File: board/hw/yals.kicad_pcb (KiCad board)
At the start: 2 copper layers, 30 parts, among them J1 SWD, J2 UART, U1 RP2040, U2 M24C02-FMN, U3 MCP1703Ax-330xxTT, U4 W25Q32JVSS, Y1 Crystal

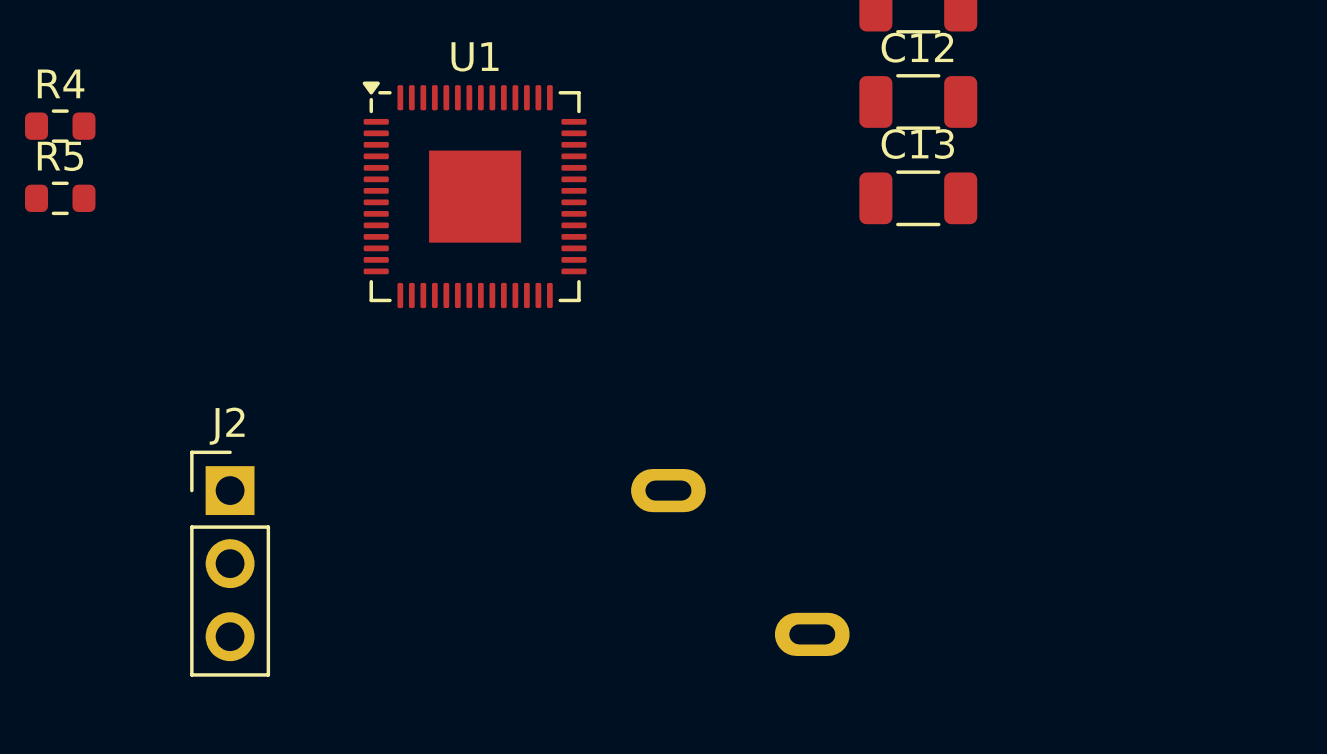
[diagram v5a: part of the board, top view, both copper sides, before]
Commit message: added engine driver with votage measuring resistor to schematics
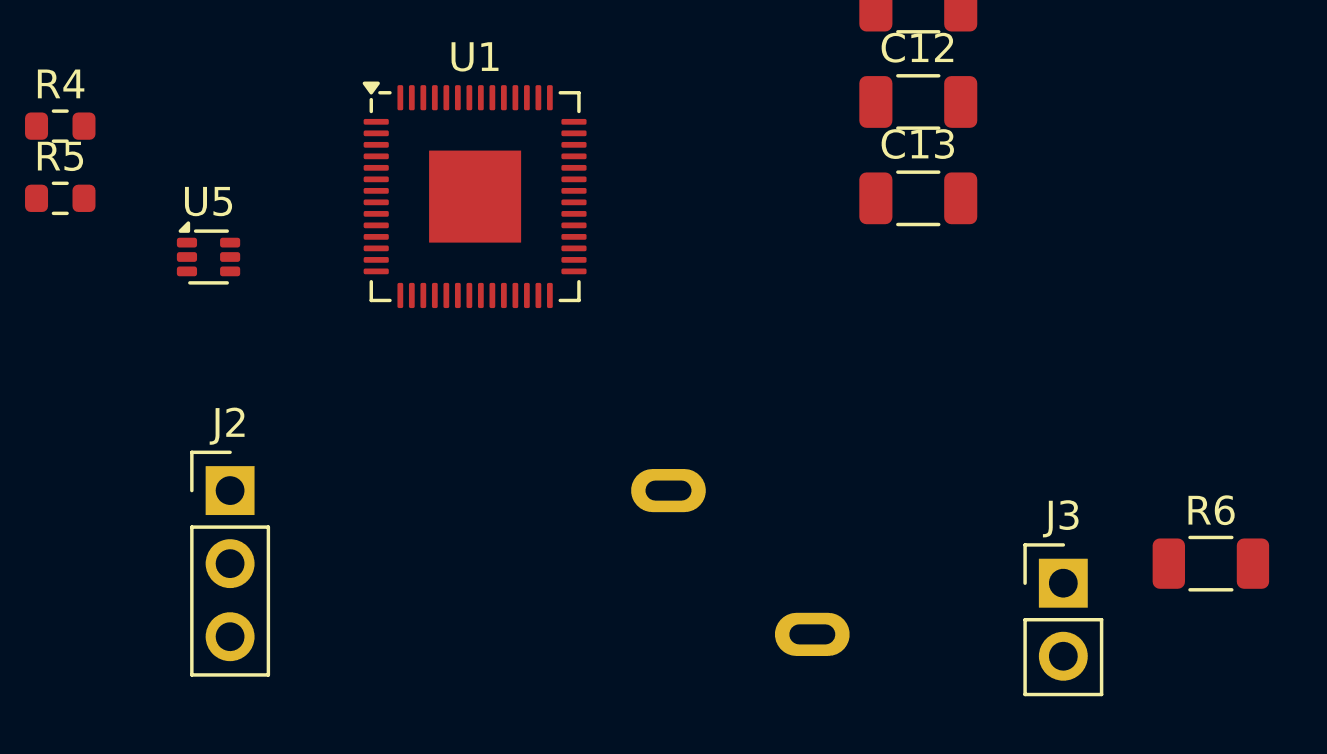
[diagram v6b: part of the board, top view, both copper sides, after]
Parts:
- added J3: eng, Connector_PinHeader_2.54mm:PinHeader_1x02_P2.54mm_Vertical, F.Cu at (183.9, 87.0)
- added R6: 0.01R, Resistor_SMD:R_1206_3216Metric, F.Cu at (189.0, 86.4)
- added U5: DRV8220, Package_TO_SOT_SMD:SOT-563, F.Cu at (154.2, 75.7)
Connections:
- U1 pad 4: /microcontroller/engine_IN1 -> /engine ctrl/eng_IN1
- U1 pad 5: /microcontroller/engine_IN2 -> /engine ctrl/eng_IN2

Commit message: fixed feedback pins directions
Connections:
- U1 pad 40: unconnected-(U1-GPIO28_ADC2-Pad40) -> /microcontroller/eng_current_feedback
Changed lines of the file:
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@@
   (net 23 "Net-(U1-QSPI_SD3)")
   (net 24 "/engine ctrl/eng_Vcc_feedback")
-  (net 25 "unconnected-(U1-GPIO28_ADC2-Pad40)")
+  (net 25 "/microcontroller/eng_current_feedback")
   (net 26 "unconnected-(U1-GPIO29_ADC3-Pad41)")
   (net 27 "unconnected-(U1-USB_DM-Pad46)")
@@
       (net 24 "/engine ctrl/eng_Vcc_feedback") (pinfunction "GPIO27_ADC1") (pintype "bidirectional"))
     (pad "40" smd roundrect (at 3.4375 -1.8) (size 0.875 0.2) (layers "F.Cu" "F.Paste" "F.Mask") (roundrect_rratio 0.25)
-      (net 25 "unconnected-(U1-GPIO28_ADC2-Pad40)") (pinfunction "GPIO28_ADC2") (pintype "bidirectional"))
+      (net 25 "/microcontroller/eng_current_feedback") (pinfunction "GPIO28_ADC2") (pintype "bidirectional"))
     (pad "41" smd roundrect (at 3.4375 -2.2) (size 0.875 0.2) (layers "F.Cu" "F.Paste" "F.Mask") (roundrect_rratio 0.25)
       (net 26 "unconnected-(U1-GPIO29_ADC3-Pad41)") (pinfunction "GPIO29_ADC3") (pintype "bidirectional"))

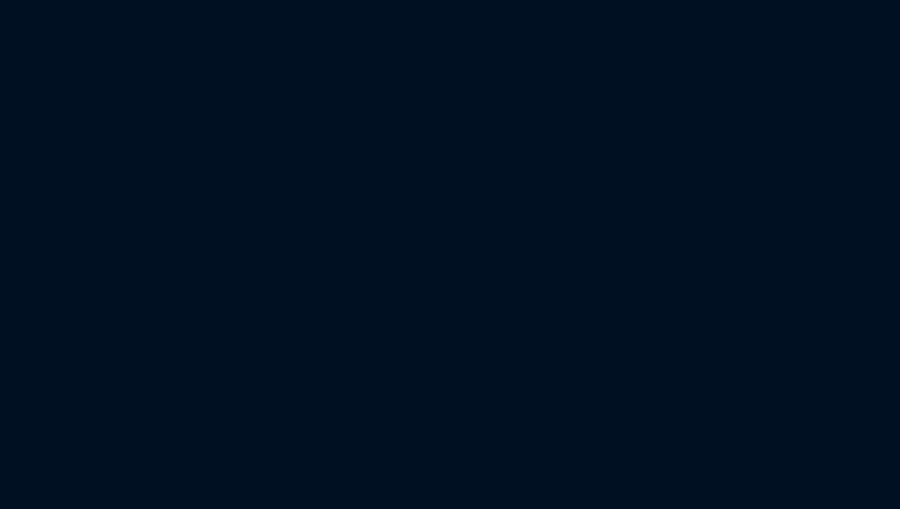
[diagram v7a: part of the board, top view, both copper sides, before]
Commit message: added current measuing circuit
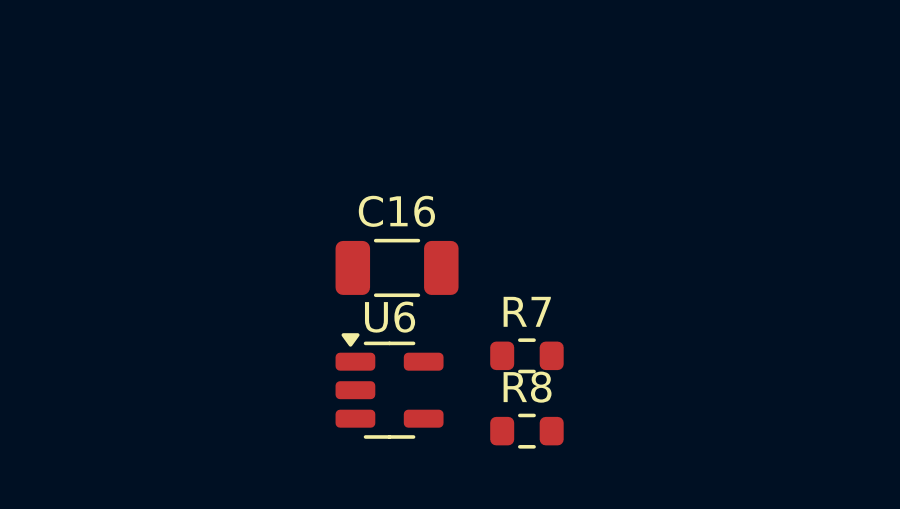
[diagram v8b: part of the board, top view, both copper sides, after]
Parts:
- added C16: 10nF, Capacitor_SMD:C_1206_3216Metric, F.Cu at (172.6, 106.3)
- added R7: 100k, Resistor_SMD:R_0603_1608Metric, F.Cu at (177.0, 109.2)
- added R8: 3.3k, Resistor_SMD:R_0603_1608Metric, F.Cu at (177.0, 111.8)
- added U6: LM321, Package_TO_SOT_SMD:SOT-23-5, F.Cu at (172.4, 110.4)
- R5: value 100k -> 20k
- R6: value 0.01R -> 0.1R
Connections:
- U1 pad 40: /microcontroller/eng_current_feedback -> /engine ctrl/eng_current_feedback
